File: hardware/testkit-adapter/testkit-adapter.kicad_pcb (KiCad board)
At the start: 2 copper layers, 100 x 100 mm, 27 parts, among them J1 LEFT, J2 RIGHT, J3 SWD, J4 Left, J5 Bottom, J6 Right

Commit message: hardware: prepare testkit adapter for manufacturing
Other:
- net class 12V added: clearance 0.3, trace_width 0.4, via_dia 0.8, via_drill 0.5
- net class 3.3V added: clearance 0.2, trace_width 0.25, via_dia 0.7, via_drill 0.3
- net class Absolute minimum added: clearance 0.15, trace_width 0.15, via_dia 0.7, via_drill 0.3
- net class Analog added: clearance 0.2, trace_width 0.2, via_dia 0.7, via_drill 0.3
- net class Default: clearance 0.2 -> 0.17; trace_width 0.2 -> 0.16; via_dia 0.8 -> 0.7; via_drill 0.4 -> 0.3
- rule pad_to_mask_clearance: 0.05 -> 0.0508
- rule trace_clearance: 0.2 -> 0.17
- rule trace_min: 0.2 -> 0.15
- rule via_min_size: 0.4 -> 0.5

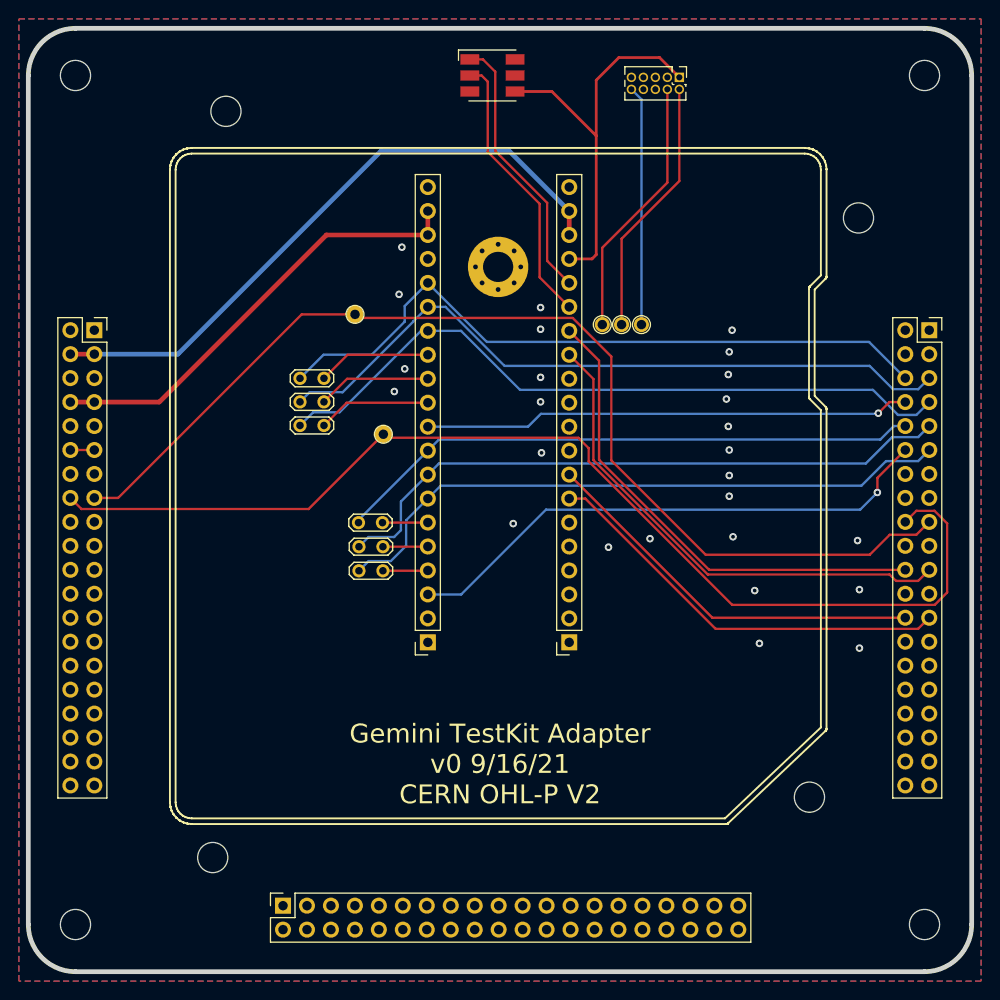
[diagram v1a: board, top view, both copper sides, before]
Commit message: hardware/testkit-adapter: Add laser designs for pin holder, board guide, and pressure plate
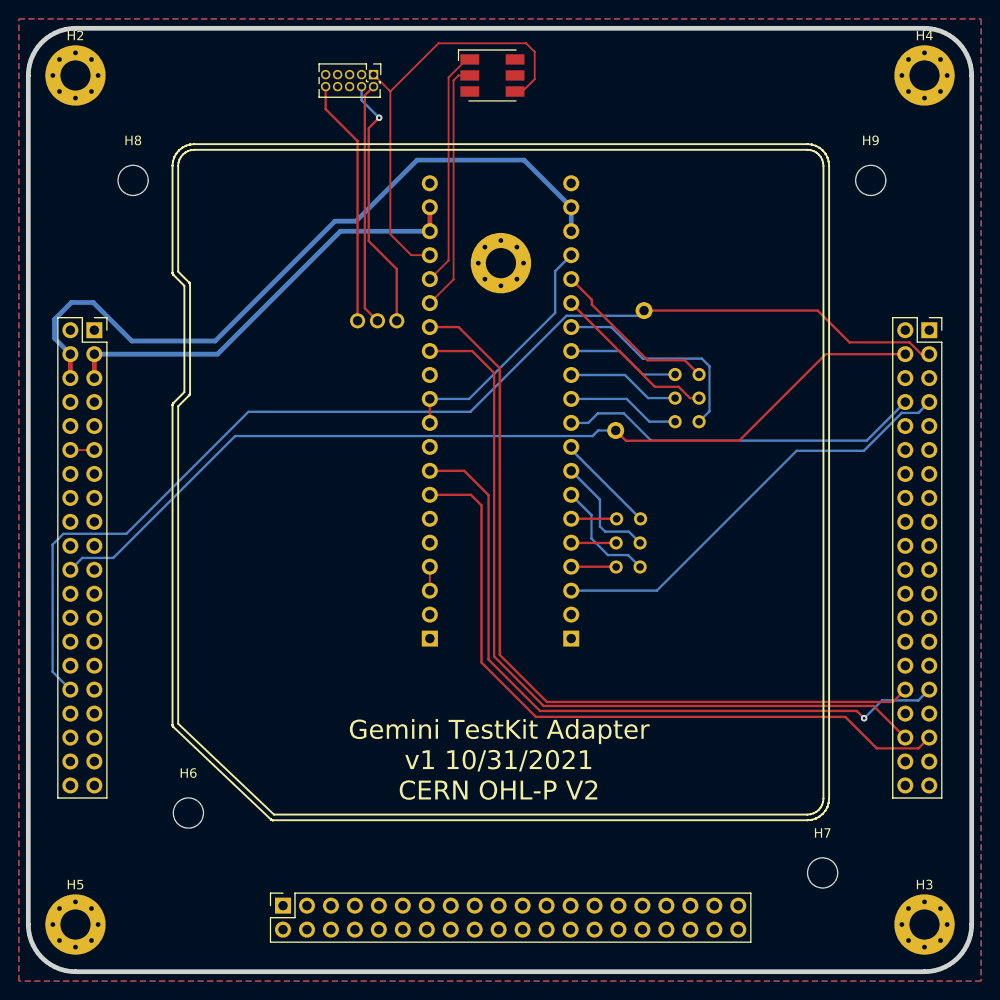
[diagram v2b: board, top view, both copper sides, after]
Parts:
- H1, J1, J2, JP1, JP2, JP3, JP4, JP5, JP6, TP1, TP2, TP3, TP4, TP5: moved to B.Cu
- H2, H3, H4, H5: footprint MountingHole:MountingHole_3.2mm_M3 -> MountingHole:MountingHole_3.2mm_M3_Pad_Via
- moved H8 77.0 mm to (86.1, 65.1)
- moved H6 74.5 mm to (92.0, 132.2)
- moved H9 65.7 mm to (164.3, 65.1)
- moved H7 64.7 mm to (159.2, 138.5)
- moved JP1 42.3 mm to (146.1, 85.7), turned to 180 degrees
- moved JP2 42.3 mm to (146.1, 88.2), turned to 180 degrees
- moved JP3 42.3 mm to (146.1, 90.7), turned to 180 degrees
- moved J3 32.4 mm to (111.6, 53.9)
- moved TP4 30.6 mm to (140.3, 78.9), turned to 180 degrees
- moved TP3 30.1 mm to (109.9, 80.0), turned to 180 degrees
- moved JP4 29.9 mm to (139.9, 101.0), turned to 180 degrees
- moved JP5 29.8 mm to (139.8, 103.5), turned to 180 degrees
- moved JP6 29.8 mm to (139.8, 106.1), turned to 180 degrees
- moved TP2 25.9 mm to (112.0, 80.0), turned to 180 degrees
- moved TP5 24.6 mm to (137.3, 91.6), turned to 180 degrees
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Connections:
- net A10* renamed ADC_1C
- net A11* renamed ADC_4B
- net A12* renamed ADC_4A
- net A15 renamed ADC_3B
- net A17 renamed ADC_3C
- net A18 renamed ADC_3D
- net A19 renamed ADC_2A
- net A20 renamed ADC_2B
- net A3* renamed Net-(J4-Pad17)
- net A4* renamed Net-(J4-Pad18)
- net A7* renamed ADC_1B
- net A9* renamed ADC_1D
- net AUDIO_IN_2D renamed EXT_AUDIO_B
- net Net-(J4-Pad37) renamed ADC_2D
- net Net-(J4-Pad38) renamed ADC_2C
- net OSC_C renamed EXT_INST_C
- net OSC_D renamed EXT_INST_D
- net SERIAL1.0 renamed Net-(J5-Pad23)
- net SERIAL1.1 renamed Net-(J5-Pad25)
- net SERIAL1.2 renamed Net-(J5-Pad27)
- H2 pad 1: Net-(H2-Pad1) -> GND
- H3 pad 1: Net-(H3-Pad1) -> GND
- H4 pad 1: Net-(H4-Pad1) -> GND
- H5 pad 1: Net-(H5-Pad1) -> GND
- J1 pad 14: AUDIO_IN_2C -> /pollux_sub
- J1 pad 15: AUDIO_IN_2B -> /pollux_pwm
- J1 pad 16: AUDIO_IN_2A -> /pollux_ramp
- J1 pad 3: AUDIO_IN_1D -> EXT_AUDIO_A
- J1 pad 7: AUDIO_IN_1C -> /castor_sub
- J1 pad 8: AUDIO_IN_1B -> /castor_pwm
- J1 pad 9: AUDIO_IN_1A -> /castor_ramp
- J2 pad 10: /duty_b_pot -> /board_3v3a
- J2 pad 11: /duty_a_pot -> /board_3v3a
- J2 pad 13: DAC_2B -> DAC_4A
- J2 pad 14: DAC_2A -> DAC_1A
- J2 pad 4: /mix_pot_out -> /mix_pot_in
- J2 pad 7: DAC_1B -> DAC_4B
- J2 pad 8: DAC_1A -> DAC_1B
- J4 pad 15: A1* -> Net-(J4-Pad15)
- J4 pad 16: A2* -> Net-(J4-Pad16)
- J4 pad 19: A5* -> GND
- J4 pad 20: A6* -> GND
- J4 pad 22: A8* -> ADC_1A
- J4 pad 27: GND -> ADC_4D
- J4 pad 28: GND -> ADC_4C
- J4 pad 29: A13 -> GND
- J4 pad 30: A14 -> GND
- J4 pad 32: A16 -> ADC_3A
- J4 pad 4: +12V -> -12V
- J4 pad 5: GND -> +12V
- J4 pad 6: GND -> -12V
- J4 pad 7: -12V -> Net-(J4-Pad7)
- J4 pad 8: -12V -> Net-(J4-Pad8)
- J5 pad 10: GND -> Net-(J5-Pad10)
- J5 pad 11: Net-(J5-Pad11) -> GND
- J5 pad 14: GND -> Net-(J5-Pad14)
- J5 pad 16: GND -> Net-(J5-Pad16)
- J5 pad 17: Net-(J5-Pad17) -> GND
- J5 pad 19: Net-(J5-Pad19) -> GND
- J5 pad 21: GND -> Net-(J5-Pad21)
- J5 pad 22: GND -> Net-(J5-Pad22)
- J5 pad 24: GND -> Net-(J5-Pad24)
- J5 pad 26: GND -> Net-(J5-Pad26)
- J5 pad 29: SERIAL1.3 -> GND
- J5 pad 3: GND -> Net-(J5-Pad3)
- J5 pad 31: Net-(J5-Pad31) -> DAC_3D
- J5 pad 32: GND -> DAC_3C
- J5 pad 33: Net-(J5-Pad33) -> DAC_3B
- J5 pad 34: GND -> DAC_3A
- J5 pad 35: Net-(J5-Pad35) -> DAC_2D
- J5 pad 36: GND -> DAC_2C
- J5 pad 37: Net-(J5-Pad37) -> DAC_2B
- J5 pad 38: GND -> DAC_2A
- J5 pad 4: GND -> Net-(J5-Pad4)
- J5 pad 5: GND -> Net-(J5-Pad5)
- J5 pad 6: GND -> Net-(J5-Pad6)
- J5 pad 8: GND -> Net-(J5-Pad8)
- J6 pad 10: AUDIO_IN_1A -> EXT_MM_A
- J6 pad 11: AUDIO_IN_1C -> EXT_FG_A
- J6 pad 12: AUDIO_IN_1D -> EXT_FG_B
- J6 pad 13: GND -> EXT_INST_A
- J6 pad 14: GND -> EXT_INST_B
- J6 pad 17: A1* -> GND
- J6 pad 18: A2* -> GND
- J6 pad 19: GND -> Net-(J6-Pad19)
- J6 pad 20: GND -> Net-(J6-Pad20)
- J6 pad 21: DAC_2B -> Net-(J6-Pad21)
- J6 pad 22: DAC_2A -> Net-(J6-Pad22)
- J6 pad 23: DAC_2C -> Net-(J6-Pad23)
- J6 pad 24: DAC_2D -> GND
- J6 pad 25: DAC_1B -> Net-(J6-Pad25)
- J6 pad 26: DAC_1A -> Net-(J6-Pad26)
- J6 pad 27: DAC_1C -> Net-(J6-Pad27)
- J6 pad 28: DAC_1D -> Net-(J6-Pad28)
- J6 pad 3: AUDIO_OUT_L -> ADC_3A
- J6 pad 31: DAC_4B -> DAC_1B
- J6 pad 32: DAC_4A -> DAC_1A
- J6 pad 33: DAC_4C -> DAC_1D
- J6 pad 34: DAC_4D -> DAC_1C
- J6 pad 35: DAC_3B -> DAC_4B
- J6 pad 36: DAC_3A -> DAC_4A
- J6 pad 37: DAC_3C -> DAC_4D
- J6 pad 38: DAC_3D -> DAC_4C
- J6 pad 4: AUDIO_OUT_R -> ADC_1A
- J6 pad 5: AUDIO_IN_2B -> EXT_OSC_D
- J6 pad 6: AUDIO_IN_2A -> EXT_OSC_C
- J6 pad 7: AUDIO_IN_2C -> EXT_AUDIO_A
- J6 pad 9: AUDIO_IN_1B -> EXT_MM_V
- JP1 pad 1: AUDIO_IN_2A -> /pollux_ramp
- JP2 pad 1: AUDIO_IN_2B -> /pollux_pwm
- JP3 pad 1: AUDIO_IN_2C -> /pollux_sub
- JP4 pad 1: AUDIO_IN_1A -> /castor_ramp
- JP5 pad 1: AUDIO_IN_1B -> /castor_pwm
- JP6 pad 1: AUDIO_IN_1C -> /castor_sub
- TP4 pad 1: A1* -> ADC_3A
- TP5 pad 1: A2* -> ADC_1A
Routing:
- net ADC_3A: track 0.00 -> 121.3 mm
- net A2*: track 118.4 -> 0.00 mm
- net A1*: track 115.0 -> 0.00 mm
- net ADC_1A: track 0.00 -> 98.9 mm
- net DAC_4A: track 0.00 -> 85.0 mm
- net AUDIO_IN_2C: track 75.1 -> 0.00 mm
- net AUDIO_IN_2B: track 75.0 -> 0.00 mm
- net DAC_4B: track 0.00 -> 74.3 mm
- net AUDIO_IN_2A: track 73.5 -> 0.00 mm
- net AUDIO_IN_1B: track 67.5 -> 0.00 mm
- net AUDIO_IN_1C: track 67.3 -> 0.00 mm
- net AUDIO_IN_1A: track 62.4 -> 0.00 mm
- net AUDIO_IN_1D: track 57.9 -> 0.00 mm, vias 1 -> 0
- net DAC_2B: track 53.6 -> 0.00 mm
- net DAC_2A: track 52.3 -> 0.00 mm
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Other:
- board text added: "Gemini TestKit Adapter v1 10/31/2021 CERN OHL-P V2"
- board text removed: "Gemini TestKit Adapter v0 9/16/21 CERN OHL-P V2"
